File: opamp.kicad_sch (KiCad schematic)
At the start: 25 parts, among them J62 Conn_02x04_Odd_Even, J63 Conn_01x02, J64 Conn_01x02, J65 Conn_01x02, J66 Conn_01x02, J67 Conn_01x02, J68 Conn_02x04_Odd_Even, Q10 SS8050, Q11 SS8050, Q12 SS8050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

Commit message: WIP v0.2.0 changes
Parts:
- removed C62, C63, C64, C65: 1uF, Capacitor_SMD:C_0603_1608Metric_Pad1.08x0.95mm_HandSolder, symbol Device:C_Small
- removed J63: Conn_01x02, HL_Connector_Pad_2.54mm:Pad_1x02_P2.54_1.7x1.7_Rect-Rnd, symbol Connector_Generic:Conn_01x02
- removed R112, R113, R114, R115: 200k, Resistor_SMD:R_0805_2012Metric_Pad1.20x1.40mm_HandSolder, symbol Device:R
- added R34, R38, R71, R72: 1k, Resistor_SMD:R_0603_1608Metric_Pad0.98x0.95mm_HandSolder, symbol Device:R_Small
- J56: renamed from J62; value Conn_02x04_Odd_Even -> Conn_01x05; footprint HL_Connector_Pad_2.54mm:Pad_2x04_P2.54_1.7x1.7_Rect-Oct -> HL_Connector_Pad_2.54mm:Pad_1x05_P2.54_1.7x1.7_Rect-Oct; symbol Connector_Generic:Conn_02x04_Odd_Even -> Connector_Generic:Conn_01x05
- J62: renamed from J68; value Conn_02x04_Odd_Even -> Conn_01x05; footprint HL_Connector_Pad_2.54mm:Pad_2x04_P2.54_1.7x1.7_Rect-Oct -> HL_Connector_Pad_2.54mm:Pad_1x05_P2.54_1.7x1.7_Rect-Oct; symbol Connector_Generic:Conn_02x04_Odd_Even -> Connector_Generic:Conn_01x05
- RV15, RV16, RV17, RV18: LCSC (none) -> C118942; THT_LCSC C118942 -> (none)
- renumbered J64 to J58, J65 to J59, J66 to J60, J67 to J61
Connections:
- net GND: now also R34.2, R38.2, R71.2, R72.2; no longer J56.3 (Pin_3), J56.5 (Pin_5), J56.7 (Pin_7), J62.3 (Pin_3), J62.5 (Pin_5), J62.7 (Pin_7)
- net IN2: now also J56.3 (Pin_3); no longer J56.4 (Pin_4)
- net IN3: now also J56.4 (Pin_4); no longer J56.6 (Pin_6)
- net IN4: now also J56.5 (Pin_5); no longer J56.8 (Pin_8)
- net OUT1: now also RV15.1, R34.1
- net OUT2: now also J62.3 (Pin_3), RV16.1, R71.1; no longer J62.4 (Pin_4)
- net OUT3: now also J62.4 (Pin_4), RV17.1, R38.1; no longer J62.6 (Pin_6)
- net OUT4: now also J62.5 (Pin_5), RV18.1, R72.1; no longer J62.8 (Pin_8)
- net VCC renamed +12V
- no-connect marks 4 -> 0
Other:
- moved on the sheet: J58, J59, J60, J61, RV15, RV16, RV17, RV18

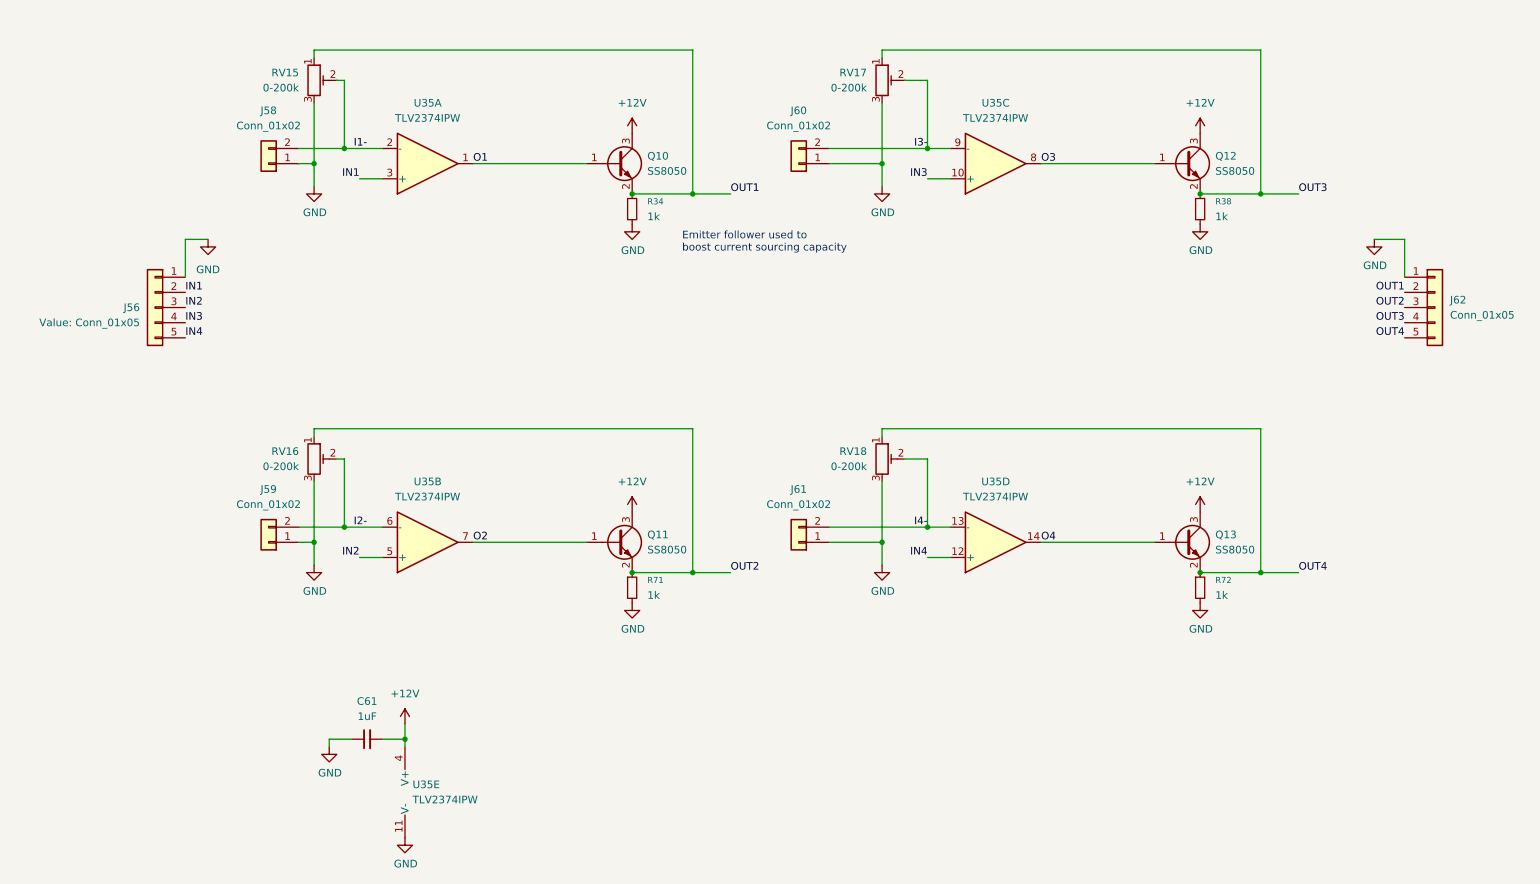
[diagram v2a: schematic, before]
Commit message: Assign part numbers and finish other 0.2.0 changes
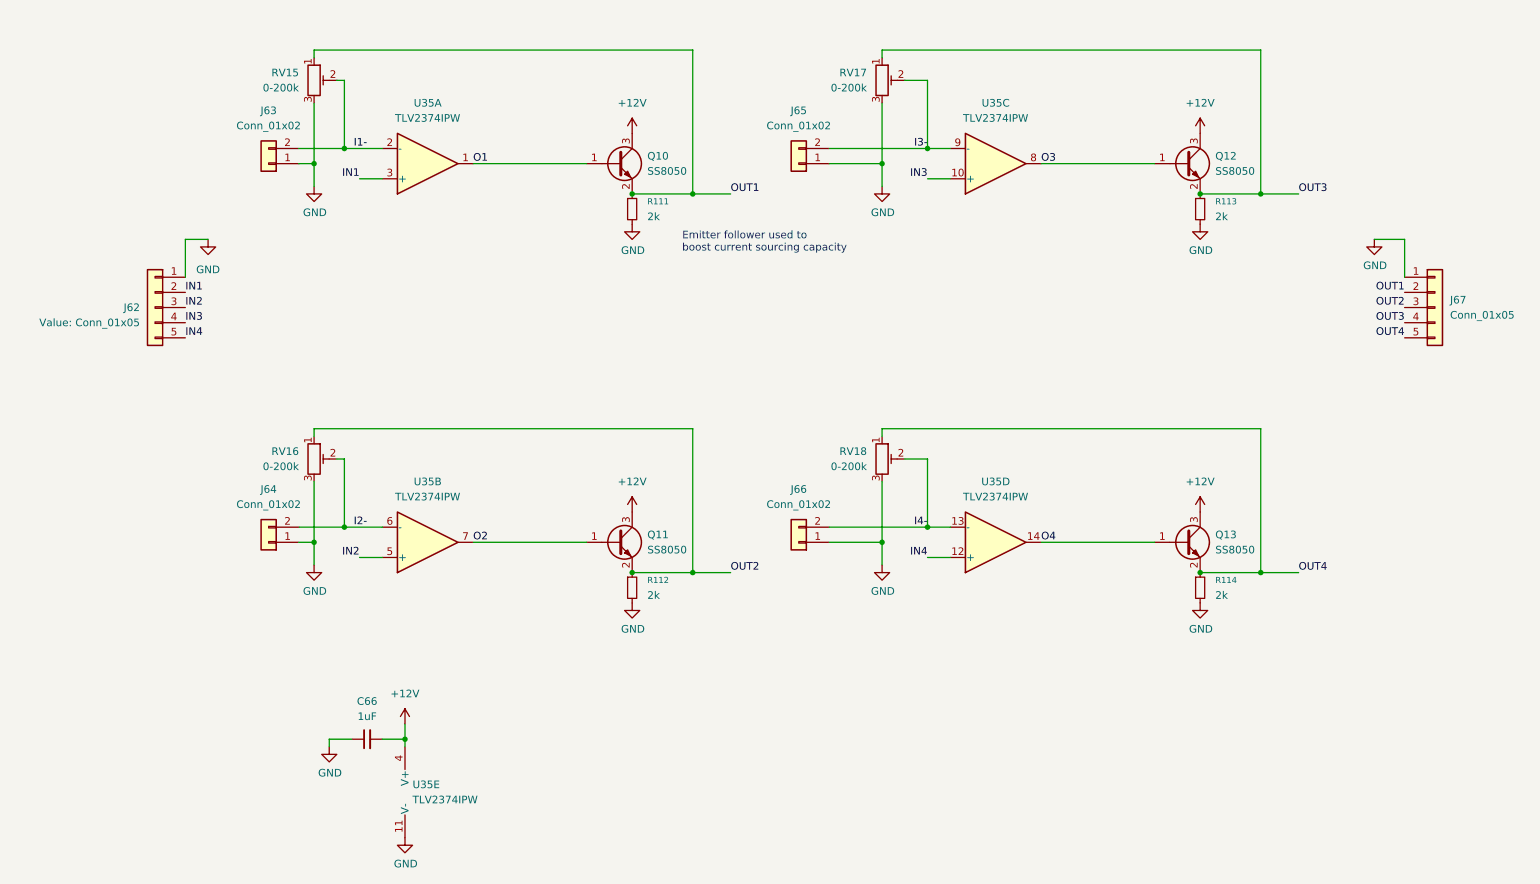
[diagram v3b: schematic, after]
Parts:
- J62: renamed from J56; LCSC (none) -> C492404
- J67: renamed from J62; LCSC (none) -> C492404
- R111: renamed from R34; value 1k -> 2k; LCSC C21190 -> C22975
- R112: renamed from R71; value 1k -> 2k; LCSC C21190 -> C22975
- R113: renamed from R38; value 1k -> 2k; LCSC C21190 -> C22975
- R114: renamed from R72; value 1k -> 2k; LCSC C21190 -> C22975
- renumbered C61 to C66, J58 to J63, J59 to J64, J60 to J65, J61 to J66

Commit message: Update the title blocks
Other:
- company: (none) -> Hat Labs Oy
- title: (none) -> HALSPA - Hat Labs Spaghetti Board
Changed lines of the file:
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@@
 	(generator_version "9.0")
 	(paper "A4")
+	(title_block
+		(title "HALSPA - Hat Labs Spaghetti Board")
+		(date "2025-04-17")
+		(rev "v0.2.0")
+		(company "Hat Labs Oy")
+		(comment 1 "See the accompanying LICENSE.md file for license details.")
+	)
 	(text "Emitter follower used to\nboost current sourcing capacity"
 		(exclude_from_sim no)

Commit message: Add JLCPCB corrections
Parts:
- J62, J67: JLCPCB_CORRECTION (none) -> 0;5.08;270
- RV15, RV16, RV17, RV18: JLCPCB_CORRECTION (none) -> 0;0;90; now in the parts list
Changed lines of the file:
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@@
 		(unit 1)
 		(exclude_from_sim no)
-		(in_bom no)
+		(in_bom yes)
 		(on_board yes)
 		(dnp no)
@@
 		)
 		(property "THT_LCSC" ""
+			(at 157.48 115.57 0)
+			(effects
+				(font
+					(size 1.27 1.27)
+				)
+				(hide yes)
+			)
+		)
+		(property "JLCPCB_CORRECTION" "0;0;90"
 			(at 157.48 115.57 0)
 			(effects
@@
 		(unit 1)
 		(exclude_from_sim no)
-		(in_bom no)
+		(in_bom yes)
 		(on_board yes)
 		(dnp no)
@@
 			)
 		)
+		(property "JLCPCB_CORRECTION" "0;0;90"
+			(at 157.48 52.07 0)
+			(effects
+				(font
+					(size 1.27 1.27)
+				)
+				(hide yes)
+			)
+		)
 		(pin "1"
 		)
@@
 		(unit 1)
 		(exclude_from_sim no)
-		(in_bom no)
+		(in_bom yes)
 		(on_board yes)
 		(dnp no)
@@
 			)
 		)
+		(property "JLCPCB_CORRECTION" "0;0;90"
+			(at 62.23 115.57 0)
+			(effects
+				(font
+					(size 1.27 1.27)
+				)
+				(hide yes)
+			)
+		)
 		(pin "1"
 		)
@@
 		)
 		(property "LCSC" "C492404"
+			(at 250.19 90.17 0)
+			(effects
+				(font
+					(size 1.27 1.27)
+				)
+				(hide yes)
+			)
+		)
+		(property "JLCPCB_CORRECTION" "0;5.08;270"
 			(at 250.19 90.17 0)
 			(effects
@@
 		(property "Value" "Conn_01x05"
 			(at 33.02 92.7099 0)
-			(show_name yes)
 			(effects
 				(font
@@
 		)
 		(property "LCSC" "C492404"
+			(at 35.56 90.17 0)
+			(effects
+				(font
+					(size 1.27 1.27)
+				)
+				(hide yes)
+			)
+		)
+		(property "JLCPCB_CORRECTION" "0;5.08;270"
 			(at 35.56 90.17 0)
 			(effects
@@
 		(unit 1)
 		(exclude_from_sim no)
-		(in_bom no)
+		(in_bom yes)
 		(on_board yes)
 		(dnp no)
@@
 			(at 62.23 52.07 0)
 			(effects
+				(font
+					(size 1.27 1.27)
+				)
+				(hide yes)
+			)
+		)
+		(property "JLCPCB_CORRECTION" "0;0;90"
+			(at 62.23 52.07 0)
+			(effects

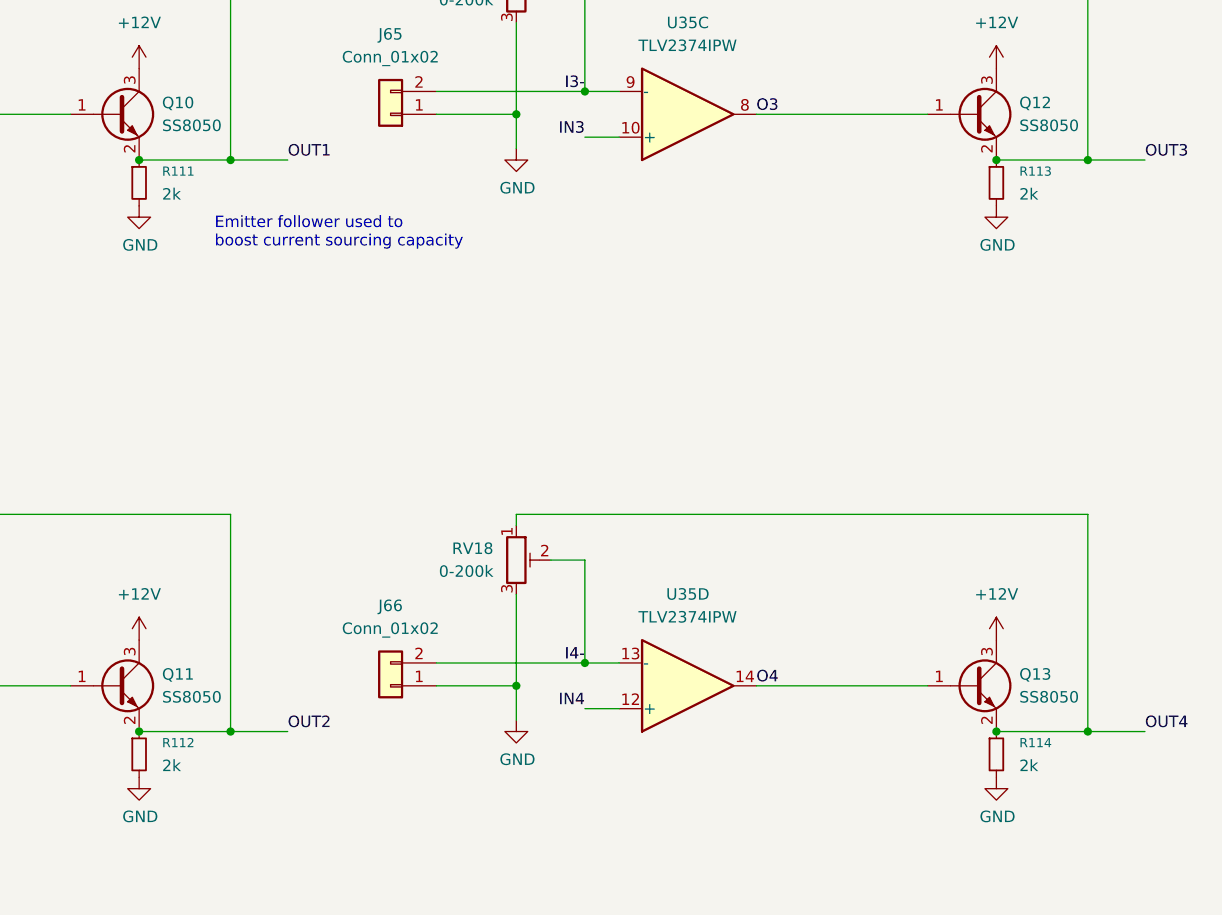
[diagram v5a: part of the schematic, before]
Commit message: Improve MCU2 layout; document curlim12v CSA
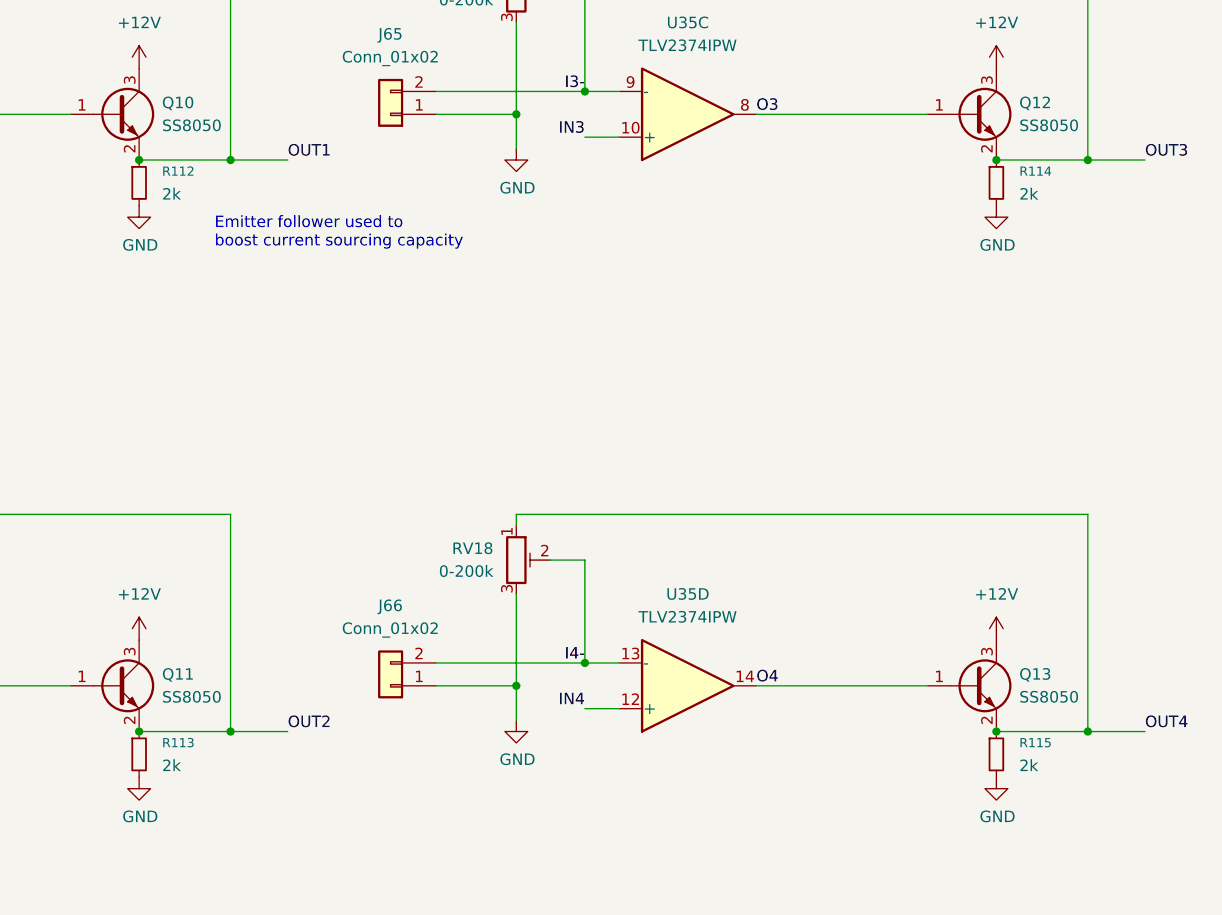
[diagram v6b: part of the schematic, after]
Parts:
- renumbered R111 to R112, R112 to R113, R113 to R114, R114 to R115
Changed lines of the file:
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@@
 		(dnp no)
 		(fields_autoplaced yes)
-		(property "Reference" "#PWR0254"
+		(property "Reference" "#PWR0255"
 			(at 115.57 128.27 0)
 			(effects
@@
 			(project "HALSPA"
 				(path "/7eeba806-440e-4671-bc07-69fe183910a7/bab37177-d1e1-4024-bdd4-a958a3dc3f62"
-					(reference "#PWR0254")
+					(reference "#PWR0255")
 					(unit 1)
 				)
@@
 		(on_board yes)
 		(dnp no)
-		(property "Reference" "#PWR0248"
+		(property "Reference" "#PWR0249"
 			(at 62.23 139.7 0)
 			(effects
@@
 			(project "HALSPA"
 				(path "/7eeba806-440e-4671-bc07-69fe183910a7/bab37177-d1e1-4024-bdd4-a958a3dc3f62"
-					(reference "#PWR0248")
+					(reference "#PWR0249")
 					(unit 1)
 				)
@@
 		(dnp no)
 		(fields_autoplaced yes)
-		(property "Reference" "R111"
+		(property "Reference" "R112"
 			(at 118.11 72.3899 0)
 			(effects
@@
 			(project ""
 				(path "/7eeba806-440e-4671-bc07-69fe183910a7/bab37177-d1e1-4024-bdd4-a958a3dc3f62"
-					(reference "R111")
+					(reference "R112")
 					(unit 1)
 				)
@@
 		(dnp no)
 		(fields_autoplaced yes)
-		(property "Reference" "#PWR0246"
+		(property "Reference" "#PWR0247"
 			(at 44.45 85.09 0)
 			(effects
@@
 			(project "HALSPA"
 				(path "/7eeba806-440e-4671-bc07-69fe183910a7/bab37177-d1e1-4024-bdd4-a958a3dc3f62"
-					(reference "#PWR0246")
+					(reference "#PWR0247")
 					(unit 1)
 				)
@@
 		(on_board yes)
 		(dnp no)
-		(property "Reference" "#PWR0262"
+		(property "Reference" "#PWR0263"
 			(at 240.03 85.09 0)
 			(effects
@@
 			(project "HALSPA"
 				(path "/7eeba806-440e-4671-bc07-69fe183910a7/bab37177-d1e1-4024-bdd4-a958a3dc3f62"
-					(reference "#PWR0262")
+					(reference "#PWR0263")
 					(unit 1)
 				)
@@
 		(dnp no)
 		(fields_autoplaced yes)
-		(property "Reference" "#PWR0252"
+		(property "Reference" "#PWR0253"
 			(at 115.57 64.77 0)
 			(effects
@@
 			(project "HALSPA"
 				(path "/7eeba806-440e-4671-bc07-69fe183910a7/bab37177-d1e1-4024-bdd4-a958a3dc3f62"
-					(reference "#PWR0252")
+					(reference "#PWR0253")
 					(unit 1)
 				)
@@
 		(on_board yes)
 		(dnp no)
-		(property "Reference" "#PWR0253"
+		(property "Reference" "#PWR0254"
 			(at 115.57 82.55 0)
 			(effects
@@
 			(project "HALSPA"
 				(path "/7eeba806-440e-4671-bc07-69fe183910a7/bab37177-d1e1-4024-bdd4-a958a3dc3f62"
-					(reference "#PWR0253")
+					(reference "#PWR0254")
 					(unit 1)
 				)
@@
 		(dnp no)
 		(fields_autoplaced yes)
-		(property "Reference" "R112"
+		(property "Reference" "R113"
 			(at 118.11 135.8899 0)
 			(effects
@@
 			(project "HALSPA"
 				(path "/7eeba806-440e-4671-bc07-69fe183910a7/bab37177-d1e1-4024-bdd4-a958a3dc3f62"
-					(reference "R112")
+					(reference "R113")
 					(unit 1)
 				)
@@
 		(dnp no)
 		(fields_autoplaced yes)
-		(property "Reference" "#PWR0260"
+		(property "Reference" "#PWR0261"
 			(at 210.82 128.27 0)
 			(effects
@@
 			(project "HALSPA"
 				(path "/7eeba806-440e-4671-bc07-69fe183910a7/bab37177-d1e1-4024-bdd4-a958a3dc3f62"
-					(reference "#PWR0260")
+					(reference "#PWR0261")
 					(unit 1)
 				)
@@
 		(dnp no)
 		(fields_autoplaced yes)
-		(property "Reference" "R114"
+		(property "Reference" "R115"
 			(at 213.36 135.8899 0)
 			(effects
@@
 			(project "HALSPA"
 				(path "/7eeba806-440e-4671-bc07-69fe183910a7/bab37177-d1e1-4024-bdd4-a958a3dc3f62"
-					(reference "R114")
+					(reference "R115")
 					(unit 1)
 				)
@@
 		(on_board yes)
 		(dnp no)
-		(property "Reference" "#PWR0249"
+		(property "Reference" "#PWR0250"
 			(at 64.77 170.18 0)
 			(effects
@@
 			(project "HALSPA"
 				(path "/7eeba806-440e-4671-bc07-69fe183910a7/bab37177-d1e1-4024-bdd4-a958a3dc3f62"
-					(reference "#PWR0249")
+					(reference "#PWR0250")
 					(unit 1)
 				)
@@
 		(on_board yes)
 		(dnp no)
-		(property "Reference" "#PWR0255"
+		(property "Reference" "#PWR0256"
 			(at 115.57 146.05 0)
 			(effects
@@
 			(project "HALSPA"
 				(path "/7eeba806-440e-4671-bc07-69fe183910a7/bab37177-d1e1-4024-bdd4-a958a3dc3f62"
-					(reference "#PWR0255")
+					(reference "#PWR0256")
 					(unit 1)
 				)
@@
 		(on_board yes)
 		(dnp no)
-		(property "Reference" "#PWR0251"
+		(property "Reference" "#PWR0252"
 			(at 77.47 185.42 0)
 			(effects
@@
 			(project "HALSPA"
 				(path "/7eeba806-440e-4671-bc07-69fe183910a7/bab37177-d1e1-4024-bdd4-a958a3dc3f62"
-					(reference "#PWR0251")
+					(reference "#PWR0252")
 					(unit 1)
 				)
@@
 		(dnp no)
 		(fields_autoplaced yes)
-		(property "Reference" "#PWR0258"
+		(property "Reference" "#PWR0259"
 			(at 210.82 64.77 0)
 			(effects
@@
 			(project "HALSPA"
 				(path "/7eeba806-440e-4671-bc07-69fe183910a7/bab37177-d1e1-4024-bdd4-a958a3dc3f62"
-					(reference "#PWR0258")
+					(reference "#PWR0259")
 					(unit 1)
 				)
@@
 		(dnp no)
 		(fields_autoplaced yes)
-		(property "Reference" "#PWR0250"
+		(property "Reference" "#PWR0251"
 			(at 77.47 163.83 0)
 			(effects
@@
 			(project ""
 				(path "/7eeba806-440e-4671-bc07-69fe183910a7/bab37177-d1e1-4024-bdd4-a958a3dc3f62"
-					(reference "#PWR0250")
+					(reference "#PWR0251")
 					(unit 1)
 				)
@@
 		(on_board yes)
 		(dnp no)
-		(property "Reference" "#PWR0256"
+		(property "Reference" "#PWR0257"
 			(at 157.48 76.2 0)
 			(effects
@@
 			(project "HALSPA"
 				(path "/7eeba806-440e-4671-bc07-69fe183910a7/bab37177-d1e1-4024-bdd4-a958a3dc3f62"
-					(reference "#PWR0256")
+					(reference "#PWR0257")
 					(unit 1)
 				)
@@
 		(on_board yes)
 		(dnp no)
-		(property "Reference" "#PWR0257"
+		(property "Reference" "#PWR0258"
 			(at 157.48 139.7 0)
 			(effects
@@
 			(project "HALSPA"
 				(path "/7eeba806-440e-4671-bc07-69fe183910a7/bab37177-d1e1-4024-bdd4-a958a3dc3f62"
-					(reference "#PWR0257")
+					(reference "#PWR0258")
 					(unit 1)
 				)
@@
 		(on_board yes)
 		(dnp no)
-		(property "Reference" "#PWR0261"
+		(property "Reference" "#PWR0262"
 			(at 210.82 146.05 0)
 			(effects
@@
 			(project "HALSPA"
 				(path "/7eeba806-440e-4671-bc07-69fe183910a7/bab37177-d1e1-4024-bdd4-a958a3dc3f62"
-					(reference "#PWR0261")
+					(reference "#PWR0262")
 					(unit 1)
 				)
@@
 		(on_board yes)
 		(dnp no)
-		(property "Reference" "#PWR0259"
+		(property "Reference" "#PWR0260"
 			(at 210.82 82.55 0)
 			(effects
@@
 			(project "HALSPA"
 				(path "/7eeba806-440e-4671-bc07-69fe183910a7/bab37177-d1e1-4024-bdd4-a958a3dc3f62"
-					(reference "#PWR0259")
+					(reference "#PWR0260")
 					(unit 1)
 				)
@@
 		(on_board yes)
 		(dnp no)
-		(property "Reference" "#PWR0247"
+		(property "Reference" "#PWR0248"
 			(at 62.23 76.2 0)
 			(effects
@@
 			(project "HALSPA"
 				(path "/7eeba806-440e-4671-bc07-69fe183910a7/bab37177-d1e1-4024-bdd4-a958a3dc3f62"
-					(reference "#PWR0247")
+					(reference "#PWR0248")
 					(unit 1)
 				)
@@
 		(dnp no)
 		(fields_autoplaced yes)
-		(property "Reference" "R113"
+		(property "Reference" "R114"
 			(at 213.36 72.3899 0)
 			(effects
@@
 			(project "HALSPA"
 				(path "/7eeba806-440e-4671-bc07-69fe183910a7/bab37177-d1e1-4024-bdd4-a958a3dc3f62"
-					(reference "R113")
+					(reference "R114")
 					(unit 1)
 				)
